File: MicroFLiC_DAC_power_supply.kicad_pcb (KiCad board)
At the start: 2 copper layers, 49.8 x 49.8 mm, 69 parts, among them P1 Socket_1x2, P2 Header_1x2, P3 Socket_2x4, U1 AP1117E50, U2 AP1117, U3 AP1117, U4 LM317, U5 LM317

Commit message: Fixed LDO feedback resistors and capacitors
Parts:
- C21, C22: value 10u/6.3V -> 4u7/25V
- C23, C24: value 10u/6.3V -> 1u/50V
- R1, R2: value 150 -> 750
- R3, R4: value 150 -> 2k1
- R5, R6: value 750 -> 150
- R7, R8: value 2k1 -> 150
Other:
- board text removed: "-5V"
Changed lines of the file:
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@@
-(kicad_pcb (version 4) (host pcbnew "(2015-12-10 BZR 6367)-product")
+(kicad_pcb (version 4) (host pcbnew 4.0.1-3.201512221402+6198~38~ubuntu14.04.1-stable)
   (general
     (links 130)
@@
   )
   (setup
-    (last_trace_width 0.508)
+    (last_trace_width 0.254)
     (user_trace_width 0.381)
     (user_trace_width 0.508)
@@
       (effects (font (size 1 1) (thickness 0.15)))
     )
-    (fp_text value 150 (at 0 2.1) (layer F.Fab) hide
+    (fp_text value 750 (at 0 2.1) (layer F.Fab) hide
       (effects (font (size 1 1) (thickness 0.15)))
     )
@@
       (effects (font (size 1 1) (thickness 0.15)) (justify mirror))
     )
-    (fp_text value 150 (at 0 -2.1) (layer B.Fab) hide
+    (fp_text value 2k1 (at 0 -2.1) (layer B.Fab) hide
       (effects (font (size 1 1) (thickness 0.15)) (justify mirror))
     )
@@
       (effects (font (size 1 1) (thickness 0.15)))
     )
-    (fp_text value 150 (at 0 2.1) (layer F.Fab) hide
+    (fp_text value 2k1 (at 0 2.1) (layer F.Fab) hide
       (effects (font (size 1 1) (thickness 0.15)))
     )
@@
       (effects (font (size 1 1) (thickness 0.15)))
     )
-    (fp_text value 750 (at 0 2.1) (layer F.Fab) hide
+    (fp_text value 150 (at 0 2.1) (layer F.Fab) hide
       (effects (font (size 1 1) (thickness 0.15)))
     )
@@
       (effects (font (size 1 1) (thickness 0.15)))
     )
-    (fp_text value 2k1 (at 0 2.1 270) (layer F.Fab) hide
+    (fp_text value 150 (at 0 2.1 270) (layer F.Fab) hide
       (effects (font (size 1 1) (thickness 0.15)))
     )
@@
       (effects (font (size 1 1) (thickness 0.15)) (justify mirror))
     )
-    (fp_text value 2k1 (at 0 -2.1 270) (layer B.Fab) hide
+    (fp_text value 150 (at 0 -2.1 270) (layer B.Fab) hide
       (effects (font (size 1 1) (thickness 0.15)) (justify mirror))
     )
@@
       (effects (font (size 1 1) (thickness 0.15)) (justify mirror))
     )
-    (fp_text value 750 (at 0 -2.1 180) (layer B.Fab) hide
+    (fp_text value 150 (at 0 -2.1 180) (layer B.Fab) hide
       (effects (font (size 1 1) (thickness 0.15)) (justify mirror))
     )
@@
       (effects (font (size 1 1) (thickness 0.15)) (justify mirror))
     )
-    (fp_text value 150 (at 0 -2.1 270) (layer B.Fab) hide
+    (fp_text value 750 (at 0 -2.1 270) (layer B.Fab) hide
       (effects (font (size 1 1) (thickness 0.15)) (justify mirror))
     )
@@
       (effects (font (size 1 1) (thickness 0.15)) (justify mirror))
     )
-    (fp_text value 10u/6.3V (at 0 -2.1) (layer B.Fab) hide
+    (fp_text value 4u7/25V (at 0 -2.1) (layer B.Fab) hide
       (effects (font (size 1 1) (thickness 0.15)) (justify mirror))
     )
@@
       (effects (font (size 1 1) (thickness 0.15)) (justify mirror))
     )
-    (fp_text value 10u/6.3V (at 0 -2.1 270) (layer B.Fab) hide
+    (fp_text value 4u7/25V (at 0 -2.1 270) (layer B.Fab) hide
       (effects (font (size 1 1) (thickness 0.15)) (justify mirror))
     )
@@
       (effects (font (size 1 1) (thickness 0.15)) (justify mirror))
     )
-    (fp_text value 10u/6.3V (at 0 -2.1) (layer B.Fab) hide
+    (fp_text value 1u/50V (at 0 -2.1) (layer B.Fab) hide
       (effects (font (size 1 1) (thickness 0.15)) (justify mirror))
     )
@@
       (effects (font (size 1 1) (thickness 0.15)) (justify mirror))
     )
-    (fp_text value 10u/6.3V (at 0 -2.1 270) (layer B.Fab) hide
+    (fp_text value 1u/50V (at 0 -2.1 270) (layer B.Fab) hide
       (effects (font (size 1 1) (thickness 0.15)) (justify mirror))
     )
@@
     (effects (font (size 0.45 0.45) (thickness 0.1)) (justify mirror))
   )
-  (gr_text -5V (at 108.204 140.208 90) (layer F.SilkS)
-    (effects (font (size 0.45 0.45) (thickness 0.1)))
+  (gr_text +5V (at 108.204 140.208 90) (layer F.SilkS)
+    (effects (font (size 0.5 0.5) (thickness 0.1)))
   )
   (gr_text -19V (at 108.204 142.748 90) (layer F.SilkS)
-    (effects (font (size 0.45 0.45) (thickness 0.1)))
+    (effects (font (size 0.5 0.5) (thickness 0.1)))
   )
   (gr_text GNDA (at 108.204 145.288 90) (layer F.SilkS)
-    (effects (font (size 0.45 0.45) (thickness 0.1)))
+    (effects (font (size 0.5 0.5) (thickness 0.1)))
   )
   (gr_text +19V (at 108.204 147.828 90) (layer F.SilkS)
-    (effects (font (size 0.45 0.45) (thickness 0.1)))
+    (effects (font (size 0.5 0.5) (thickness 0.1)))
   )
   (gr_text +7.5V (at 102.108 147.828 90) (layer F.SilkS)
-    (effects (font (size 0.45 0.45) (thickness 0.1)))
+    (effects (font (size 0.5 0.5) (thickness 0.1)))
   )
   (gr_text GNDA (at 102.108 145.288 90) (layer F.SilkS)
-    (effects (font (size 0.45 0.45) (thickness 0.1)))
+    (effects (font (size 0.5 0.5) (thickness 0.1)))
   )
   (gr_text -7.5V (at 102.108 142.748 90) (layer F.SilkS)
-    (effects (font (size 0.45 0.45) (thickness 0.1)))
+    (effects (font (size 0.5 0.5) (thickness 0.1)))
   )
   (gr_text GND (at 102.108 140.208 90) (layer F.SilkS)
-    (effects (font (size 0.45 0.45) (thickness 0.1)))
+    (effects (font (size 0.5 0.5) (thickness 0.1)))
   )
   (gr_text "MicroFLIC ADC/DAC power supply v1.1\nJakub Nedbal 2016" (at 101.346 102.616) (layer F.SilkS)

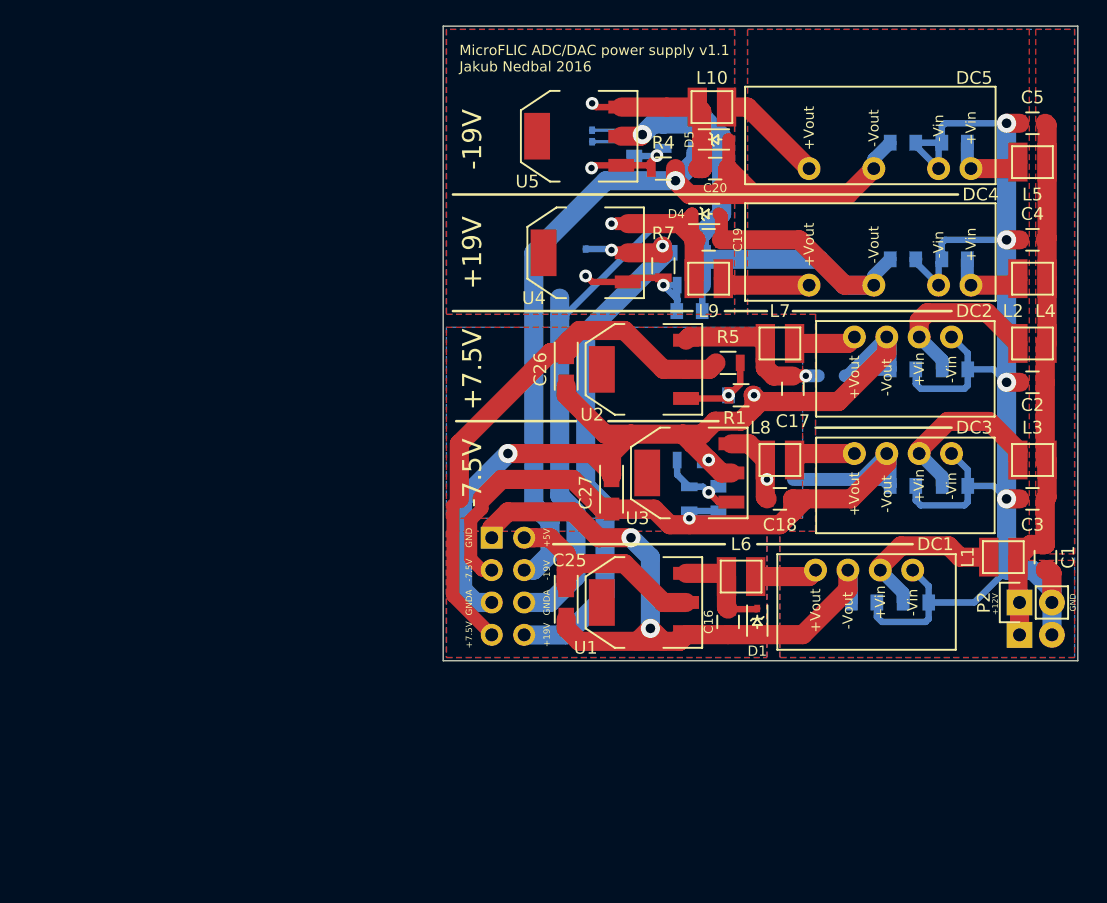
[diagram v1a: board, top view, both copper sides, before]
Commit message: Fixed power output connector orientation
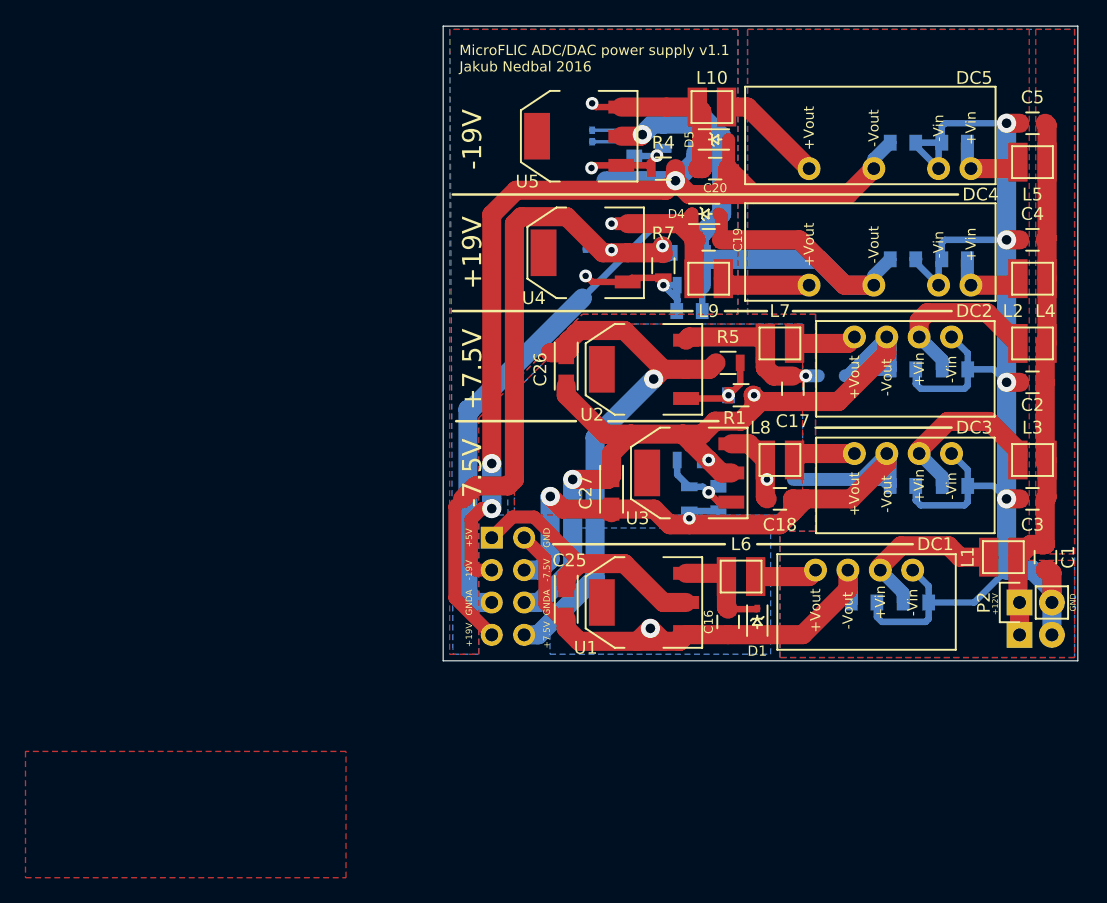
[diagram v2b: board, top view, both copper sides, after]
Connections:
- P3 pad 1: /5V_GND -> /+5V
- P3 pad 2: /+5V -> /5V_GND
- P3 pad 3: /-7.5V -> /-19V
- P3 pad 4: /-19V -> /-7.5V
- P3 pad 5: /7.5V_GND -> /19V_GND
- P3 pad 6: /19V_GND -> /7.5V_GND
- P3 pad 7: /+7.5V -> /+19V
- P3 pad 8: /+19V -> /+7.5V
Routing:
- net /5V_GND: track 53.0 -> 40.3 mm, vias 2 -> 1
- net /-19V: track 79.6 -> 90.8 mm, vias 1 -> 3
- net /7.5V_GND: track 82.6 -> 72.5 mm
- net /+19V: track 45.2 -> 54.6 mm
- net /-7.5V: track 65.0 -> 59.0 mm, vias 1 -> 2
- net /+5V: track 18.9 -> 20.9 mm
- net /+7.5V: track 44.4 -> 43.8 mm, vias 0 -> 1

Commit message: Production files for Seeedstudio
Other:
- board text added: "MicroFLIC ADC/DAC power supply v1.2 Jakub Nedbal 2016"
- board text removed: "MicroFLIC ADC/DAC power supply v1.1 Jakub Nedbal 2016"
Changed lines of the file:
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@@
   (general
     (links 130)
-    (no_connects 1)
-    (area 100.025999 100.025999 149.910001 149.910001)
+    (no_connects 0)
+    (area 99.607 100.025999 150.127 151.957)
     (thickness 1.6)
     (drawings 38)
@@
   (page A4)
   (layers
-    (0 F.Cu signal hide)
-    (31 B.Cu signal hide)
+    (0 F.Cu signal)
+    (31 B.Cu signal)
     (32 B.Adhes user)
     (33 F.Adhes user)
@@
   )
   (setup
-    (last_trace_width 1.5)
+    (last_trace_width 0.254)
     (user_trace_width 0.381)
     (user_trace_width 0.508)
@@
     (effects (font (size 0.5 0.5) (thickness 0.1)))
   )
-  (gr_text "MicroFLIC ADC/DAC power supply v1.1\nJakub Nedbal 2016" (at 101.346 102.616) (layer F.SilkS)
+  (gr_text "MicroFLIC ADC/DAC power supply v1.2\nJakub Nedbal 2016" (at 101.346 102.616) (layer F.SilkS)
     (effects (font (size 0.8 0.8) (thickness 0.12)) (justify left))
   )
@@
     (polygon
       (pts
-        (xy 92.456 166.878) (xy 92.456 156.972) (xy 67.31 156.972) (xy 67.31 166.878)
+        (xy 125.73 149.352) (xy 125.73 139.446) (xy 108.458 139.446) (xy 108.458 149.352)
       )
     )

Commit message: Fixed connector descriptions
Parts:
- P1: value Socket_1x2 -> 1x2 socket strip
- P2: value Header_1x2 -> 1x2 header strip
- P3: value Socket_2x4 -> 2x4 socket strip
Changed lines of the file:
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@@
-(kicad_pcb (version 4) (host pcbnew 4.0.1-3.201512221402+6198~38~ubuntu14.04.1-stable)
+(kicad_pcb (version 4) (host pcbnew "(2015-12-10 BZR 6367)-product")
   (general
     (links 130)
     (no_connects 0)
-    (area 99.607 100.025999 150.127 151.957)
+    (area 100.025999 100.025999 149.910001 149.910001)
     (thickness 1.6)
     (drawings 38)
@@
       (effects (font (size 1 1) (thickness 0.15)) (justify mirror))
     )
-    (fp_text value Socket_1x2 (at 0 3.1) (layer B.Fab) hide
+    (fp_text value "1x2 socket strip" (at 0 3.1) (layer B.Fab) hide
       (effects (font (size 1 1) (thickness 0.15)) (justify mirror))
     )
@@
       (effects (font (size 1 1) (thickness 0.15)) (justify mirror))
     )
-    (fp_text value Socket_2x4 (at 0 3.1 270) (layer B.Fab) hide
+    (fp_text value "2x4 socket strip" (at 0 3.1 270) (layer B.Fab) hide
       (effects (font (size 1 1) (thickness 0.15)) (justify mirror))
     )
@@
       (effects (font (size 1 1) (thickness 0.15)))
     )
-    (fp_text value Header_1x2 (at 0 -3.1 90) (layer F.Fab) hide
-      (effects (font (size 1 1) (thickness 0.15)))
-    )
+    (fp_text value "1x2 header strip" (at 0 -3.1 90) (layer F.Fab) hide
+      (effects (font (size 1 1) (thickness 0.15)))
+    )
